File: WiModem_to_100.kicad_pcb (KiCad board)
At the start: 2 copper layers, 12.3 x 34.7 mm, 2 parts, among them J1 DB25_Male, J2 DB25_Male

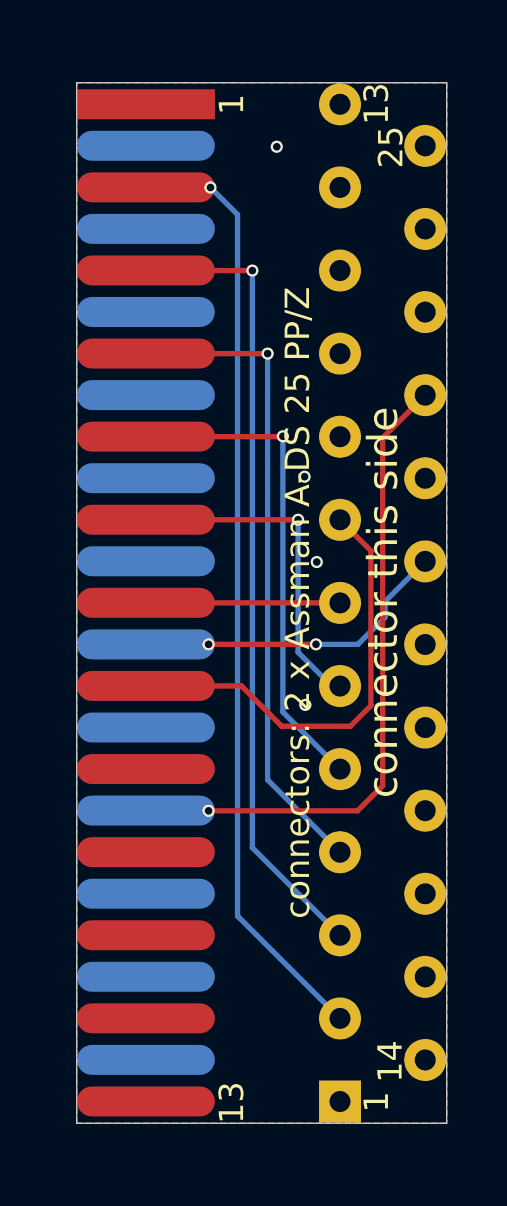
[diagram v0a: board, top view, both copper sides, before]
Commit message: tiny adjustments to routing and ground plane connections
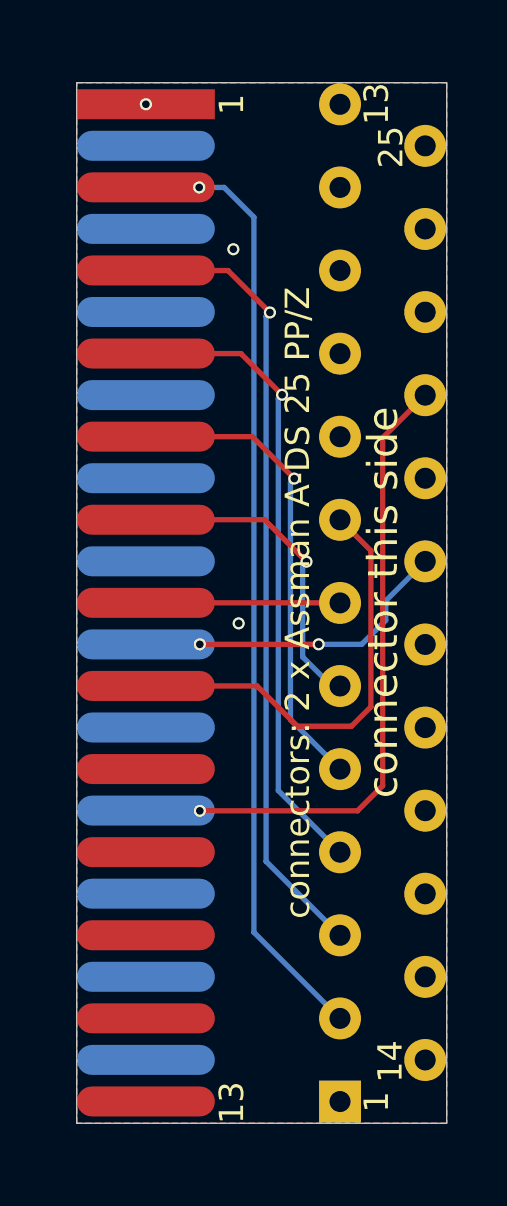
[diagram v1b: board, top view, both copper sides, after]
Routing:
- net /TXD: track 29.5 -> 31.9 mm
- net /DSR: track 10.6 -> 10.0 mm
- net /CTS: track 15.7 -> 15.2 mm
- net GND: vias 4 -> 3

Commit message: widen through-holes, improve readme
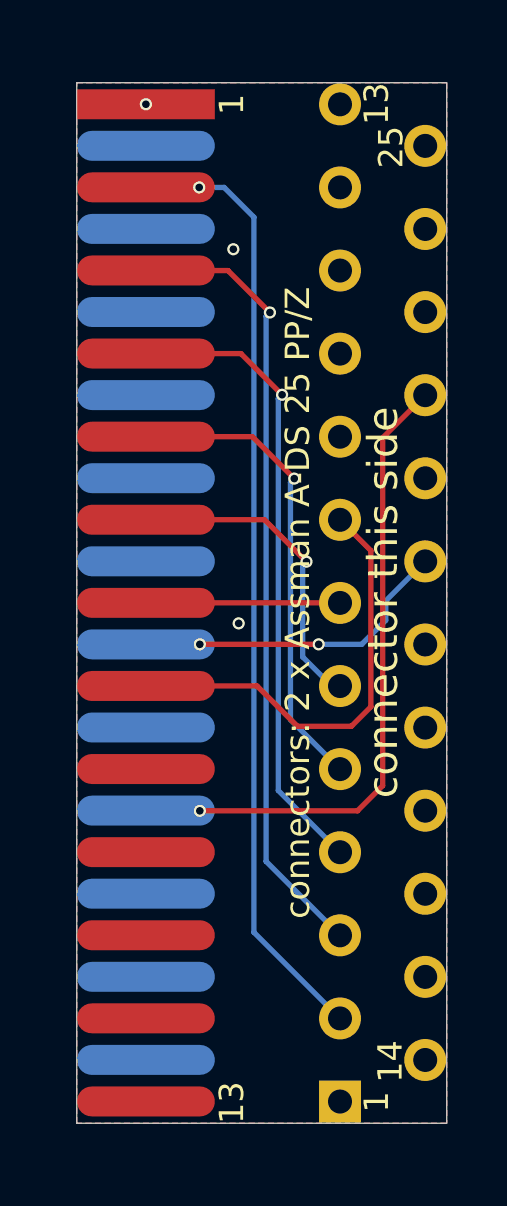
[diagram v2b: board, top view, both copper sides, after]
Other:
- rule pad_to_mask_clearance: 0.051 -> 0
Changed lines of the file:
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@@
     (35 F.Paste user hide)
     (36 B.SilkS user)
-    (37 F.SilkS user hide)
+    (37 F.SilkS user)
     (38 B.Mask user)
-    (39 F.Mask user hide)
+    (39 F.Mask user)
     (40 Dwgs.User user hide)
     (41 Cmts.User user hide)
@@
     (mod_text_size 1 1)
     (mod_text_width 0.15)
-    (pad_size 1.524 1.524)
-    (pad_drill 0.762)
-    (pad_to_mask_clearance 0.051)
-    (solder_mask_min_width 0.25)
+    (pad_size 1.4 1.4)
+    (pad_drill 0.8)
+    (pad_to_mask_clearance 0)
     (aux_axis_origin 0 0)
     (visible_elements FFFFFF7F)
@@
     (fp_arc (start 42.17 -3.83) (end 42.17 -4.83) (angle 90) (layer F.Fab) (width 0.1))
     (fp_arc (start -8.93 -3.83) (end -9.93 -3.83) (angle 90) (layer F.Fab) (width 0.1))
-    (pad 25 thru_hole circle (at 31.855 2.84 90) (size 1.4 1.4) (drill 0.7) (layers *.Cu *.Mask))
-    (pad 24 thru_hole circle (at 29.085 2.84 90) (size 1.4 1.4) (drill 0.7) (layers *.Cu *.Mask))
-    (pad 23 thru_hole circle (at 26.315 2.84 90) (size 1.4 1.4) (drill 0.7) (layers *.Cu *.Mask))
-    (pad 22 thru_hole circle (at 23.545 2.84 90) (size 1.4 1.4) (drill 0.7) (layers *.Cu *.Mask)
+    (pad 25 thru_hole circle (at 31.855 2.84 90) (size 1.4 1.4) (drill 0.8) (layers *.Cu *.Mask))
+    (pad 24 thru_hole circle (at 29.085 2.84 90) (size 1.4 1.4) (drill 0.8) (layers *.Cu *.Mask))
+    (pad 23 thru_hole circle (at 26.315 2.84 90) (size 1.4 1.4) (drill 0.8) (layers *.Cu *.Mask))
+    (pad 22 thru_hole circle (at 23.545 2.84 90) (size 1.4 1.4) (drill 0.8) (layers *.Cu *.Mask)
       (net 1 /RI))
-    (pad 21 thru_hole circle (at 20.775 2.84 90) (size 1.4 1.4) (drill 0.7) (layers *.Cu *.Mask))
-    (pad 20 thru_hole circle (at 18.005 2.84 90) (size 1.4 1.4) (drill 0.7) (layers *.Cu *.Mask)
+    (pad 21 thru_hole circle (at 20.775 2.84 90) (size 1.4 1.4) (drill 0.8) (layers *.Cu *.Mask))
+    (pad 20 thru_hole circle (at 18.005 2.84 90) (size 1.4 1.4) (drill 0.8) (layers *.Cu *.Mask)
       (net 2 /DTR))
-    (pad 19 thru_hole circle (at 15.235 2.84 90) (size 1.4 1.4) (drill 0.7) (layers *.Cu *.Mask))
-    (pad 18 thru_hole circle (at 12.465 2.84 90) (size 1.4 1.4) (drill 0.7) (layers *.Cu *.Mask))
-    (pad 17 thru_hole circle (at 9.695 2.84 90) (size 1.4 1.4) (drill 0.7) (layers *.Cu *.Mask))
-    (pad 16 thru_hole circle (at 6.925 2.84 90) (size 1.4 1.4) (drill 0.7) (layers *.Cu *.Mask))
-    (pad 15 thru_hole circle (at 4.155 2.84 90) (size 1.4 1.4) (drill 0.7) (layers *.Cu *.Mask))
-    (pad 14 thru_hole circle (at 1.385 2.84 90) (size 1.4 1.4) (drill 0.7) (layers *.Cu *.Mask))
-    (pad 13 thru_hole circle (at 33.24 0 90) (size 1.4 1.4) (drill 0.7) (layers *.Cu *.Mask))
-    (pad 12 thru_hole circle (at 30.47 0 90) (size 1.4 1.4) (drill 0.7) (layers *.Cu *.Mask))
-    (pad 11 thru_hole circle (at 27.7 0 90) (size 1.4 1.4) (drill 0.7) (layers *.Cu *.Mask))
-    (pad 10 thru_hole circle (at 24.93 0 90) (size 1.4 1.4) (drill 0.7) (layers *.Cu *.Mask))
-    (pad 9 thru_hole circle (at 22.16 0 90) (size 1.4 1.4) (drill 0.7) (layers *.Cu *.Mask))
-    (pad 8 thru_hole circle (at 19.39 0 90) (size 1.4 1.4) (drill 0.7) (layers *.Cu *.Mask)
+    (pad 19 thru_hole circle (at 15.235 2.84 90) (size 1.4 1.4) (drill 0.8) (layers *.Cu *.Mask))
+    (pad 18 thru_hole circle (at 12.465 2.84 90) (size 1.4 1.4) (drill 0.8) (layers *.Cu *.Mask))
+    (pad 17 thru_hole circle (at 9.695 2.84 90) (size 1.4 1.4) (drill 0.8) (layers *.Cu *.Mask))
+    (pad 16 thru_hole circle (at 6.925 2.84 90) (size 1.4 1.4) (drill 0.8) (layers *.Cu *.Mask))
+    (pad 15 thru_hole circle (at 4.155 2.84 90) (size 1.4 1.4) (drill 0.8) (layers *.Cu *.Mask))
+    (pad 14 thru_hole circle (at 1.385 2.84 90) (size 1.4 1.4) (drill 0.8) (layers *.Cu *.Mask))
+    (pad 13 thru_hole circle (at 33.24 0 90) (size 1.4 1.4) (drill 0.8) (layers *.Cu *.Mask))
+    (pad 12 thru_hole circle (at 30.47 0 90) (size 1.4 1.4) (drill 0.8) (layers *.Cu *.Mask))
+    (pad 11 thru_hole circle (at 27.7 0 90) (size 1.4 1.4) (drill 0.8) (layers *.Cu *.Mask))
+    (pad 10 thru_hole circle (at 24.93 0 90) (size 1.4 1.4) (drill 0.8) (layers *.Cu *.Mask))
+    (pad 9 thru_hole circle (at 22.16 0 90) (size 1.4 1.4) (drill 0.8) (layers *.Cu *.Mask))
+    (pad 8 thru_hole circle (at 19.39 0 90) (size 1.4 1.4) (drill 0.8) (layers *.Cu *.Mask)
       (net 3 /DCD))
-    (pad 7 thru_hole circle (at 16.62 0 90) (size 1.4 1.4) (drill 0.7) (layers *.Cu *.Mask)
+    (pad 7 thru_hole circle (at 16.62 0 90) (size 1.4 1.4) (drill 0.8) (layers *.Cu *.Mask)
       (net 4 /SG))
-    (pad 6 thru_hole circle (at 13.85 0 90) (size 1.4 1.4) (drill 0.7) (layers *.Cu *.Mask)
+    (pad 6 thru_hole circle (at 13.85 0 90) (size 1.4 1.4) (drill 0.8) (layers *.Cu *.Mask)
       (net 5 /DSR))
-    (pad 5 thru_hole circle (at 11.08 0 90) (size 1.4 1.4) (drill 0.7) (layers *.Cu *.Mask)
+    (pad 5 thru_hole circle (at 11.08 0 90) (size 1.4 1.4) (drill 0.8) (layers *.Cu *.Mask)
       (net 6 /CTS))
-    (pad 4 thru_hole circle (at 8.31 0 90) (size 1.4 1.4) (drill 0.7) (layers *.Cu *.Mask)
+    (pad 4 thru_hole circle (at 8.31 0 90) (size 1.4 1.4) (drill 0.8) (layers *.Cu *.Mask)
       (net 7 /RTS))
-    (pad 3 thru_hole circle (at 5.54 0 90) (size 1.4 1.4) (drill 0.7) (layers *.Cu *.Mask)
+    (pad 3 thru_hole circle (at 5.54 0 90) (size 1.4 1.4) (drill 0.8) (layers *.Cu *.Mask)
       (net 8 /RXD))
-    (pad 2 thru_hole circle (at 2.77 0 90) (size 1.4 1.4) (drill 0.7) (layers *.Cu *.Mask)
+    (pad 2 thru_hole circle (at 2.77 0 90) (size 1.4 1.4) (drill 0.8) (layers *.Cu *.Mask)
       (net 9 /TXD))
-    (pad 1 thru_hole rect (at 0 0 90) (size 1.4 1.4) (drill 0.7) (layers *.Cu *.Mask)
+    (pad 1 thru_hole rect (at 0 0 90) (size 1.4 1.4) (drill 0.8) (layers *.Cu *.Mask)
       (net 10 GND))
     (model ${KIPRJMOD}/0_LOCAL.3dshapes/connector_a-ds_25_pp_z.stp
@@
   (gr_line (start 135.4455 79.0829) (end 147.7772 79.0829) (layer Edge.Cuts) (width 0.0254))
   (gr_line (start 147.7772 113.7666) (end 147.7772 79.0829) (layer Edge.Cuts) (width 0.0254))
-  (via (at 140.6652 84.6328) (size 0.4064) (drill 0.254) (layers F.Cu B.Cu) (net 10))
   (segment (start 139.5476 103.3526) (end 144.8054 103.3526) (width 0.1778) (layer F.Cu) (net 1))
   (via (at 139.5476 103.3526) (size 0.4064) (drill 0.254) (layers F.Cu B.Cu) (net 1))
@@
   (segment (start 141.351 83.566) (end 141.351 107.4025) (width 0.1778) (layer B.Cu) (net 9))
   (segment (start 140.35786 82.57286) (end 141.351 83.566) (width 0.1778) (layer B.Cu) (net 9))
+  (via (at 140.6652 84.6328) (size 0.4064) (drill 0.254) (layers F.Cu B.Cu) (net 10))
   (via (at 140.843 97.1042) (size 0.4064) (drill 0.254) (layers F.Cu B.Cu) (net 10))
   (via (at 137.75 79.8) (size 0.4064) (drill 0.254) (layers F.Cu B.Cu) (net 10))

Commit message: edge connector too close to normal connector
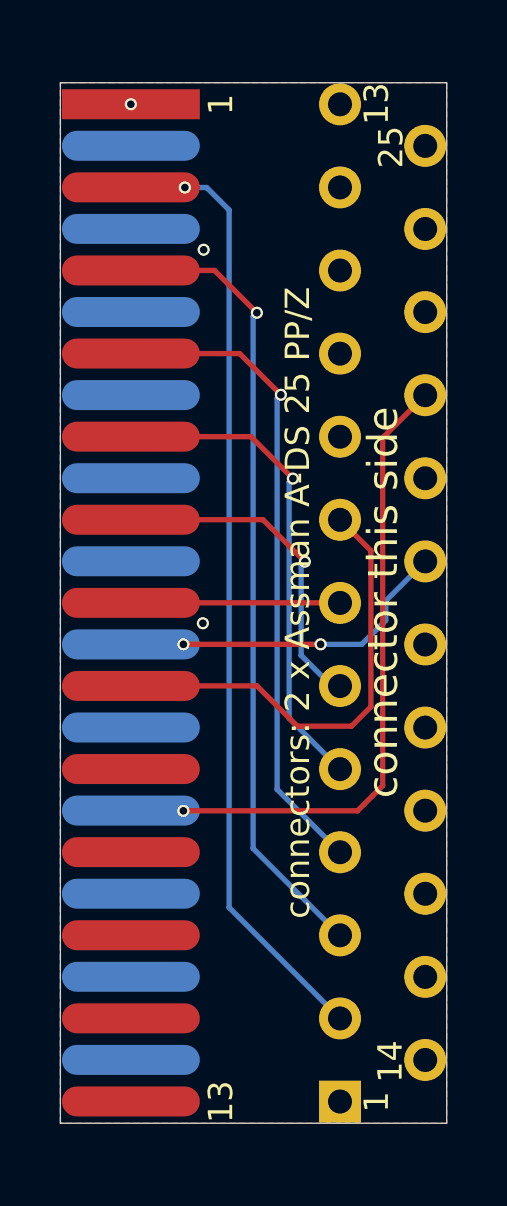
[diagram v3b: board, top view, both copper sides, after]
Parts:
- moved J1 0.50 mm to (136.8, 96.4)
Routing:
- net /RTS: track 20.5 -> 23.0 mm
- net /RXD: track 24.4 -> 26.8 mm
- net /TXD: track 31.9 -> 30.3 mm
- net /CTS: track 15.2 -> 16.4 mm
- net /DSR: track 10.0 -> 11.3 mm
- net /RI: track 20.0 -> 20.6 mm
- net /DTR: track 9.04 -> 9.59 mm
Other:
- board size 12.3 x 34.7 mm -> 12.9 x 34.7 mm

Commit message: larger drills
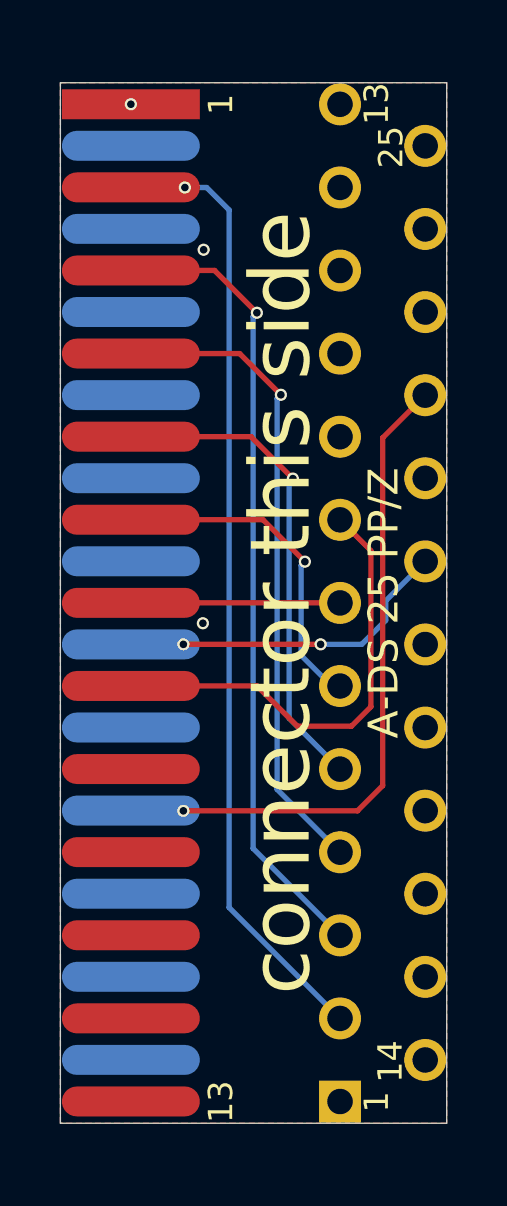
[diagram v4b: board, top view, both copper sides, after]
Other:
- board text added: "A-DS 25 PP/Z"
- board text added: "github.com/bkw777/WiModem_to_100"
- board text removed: "connectors: 2 x Assman A-DS 25 PP/Z"
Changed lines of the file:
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@@
   (general
     (thickness 1.6)
-    (drawings 20)
+    (drawings 21)
     (tracks 56)
     (zones 0)
@@
   )
   (setup
-    (last_trace_width 0.1778)
+    (last_trace_width 0.25)
     (user_trace_width 0.1778)
     (trace_clearance 0.2)
@@
     (fp_arc (start 42.17 -3.83) (end 42.17 -4.83) (angle 90) (layer F.Fab) (width 0.1))
     (fp_arc (start -8.93 -3.83) (end -9.93 -3.83) (angle 90) (layer F.Fab) (width 0.1))
-    (pad 25 thru_hole circle (at 31.855 2.84 90) (size 1.4 1.4) (drill 0.8) (layers *.Cu *.Mask))
-    (pad 24 thru_hole circle (at 29.085 2.84 90) (size 1.4 1.4) (drill 0.8) (layers *.Cu *.Mask))
-    (pad 23 thru_hole circle (at 26.315 2.84 90) (size 1.4 1.4) (drill 0.8) (layers *.Cu *.Mask))
-    (pad 22 thru_hole circle (at 23.545 2.84 90) (size 1.4 1.4) (drill 0.8) (layers *.Cu *.Mask)
+    (pad 25 thru_hole circle (at 31.855 2.84 90) (size 1.4 1.4) (drill 0.85) (layers *.Cu *.Mask))
+    (pad 24 thru_hole circle (at 29.085 2.84 90) (size 1.4 1.4) (drill 0.85) (layers *.Cu *.Mask))
+    (pad 23 thru_hole circle (at 26.315 2.84 90) (size 1.4 1.4) (drill 0.85) (layers *.Cu *.Mask))
+    (pad 22 thru_hole circle (at 23.545 2.84 90) (size 1.4 1.4) (drill 0.85) (layers *.Cu *.Mask)
       (net 1 /RI))
-    (pad 21 thru_hole circle (at 20.775 2.84 90) (size 1.4 1.4) (drill 0.8) (layers *.Cu *.Mask))
-    (pad 20 thru_hole circle (at 18.005 2.84 90) (size 1.4 1.4) (drill 0.8) (layers *.Cu *.Mask)
+    (pad 21 thru_hole circle (at 20.775 2.84 90) (size 1.4 1.4) (drill 0.85) (layers *.Cu *.Mask))
+    (pad 20 thru_hole circle (at 18.005 2.84 90) (size 1.4 1.4) (drill 0.85) (layers *.Cu *.Mask)
       (net 2 /DTR))
-    (pad 19 thru_hole circle (at 15.235 2.84 90) (size 1.4 1.4) (drill 0.8) (layers *.Cu *.Mask))
-    (pad 18 thru_hole circle (at 12.465 2.84 90) (size 1.4 1.4) (drill 0.8) (layers *.Cu *.Mask))
-    (pad 17 thru_hole circle (at 9.695 2.84 90) (size 1.4 1.4) (drill 0.8) (layers *.Cu *.Mask))
-    (pad 16 thru_hole circle (at 6.925 2.84 90) (size 1.4 1.4) (drill 0.8) (layers *.Cu *.Mask))
-    (pad 15 thru_hole circle (at 4.155 2.84 90) (size 1.4 1.4) (drill 0.8) (layers *.Cu *.Mask))
-    (pad 14 thru_hole circle (at 1.385 2.84 90) (size 1.4 1.4) (drill 0.8) (layers *.Cu *.Mask))
-    (pad 13 thru_hole circle (at 33.24 0 90) (size 1.4 1.4) (drill 0.8) (layers *.Cu *.Mask))
-    (pad 12 thru_hole circle (at 30.47 0 90) (size 1.4 1.4) (drill 0.8) (layers *.Cu *.Mask))
-    (pad 11 thru_hole circle (at 27.7 0 90) (size 1.4 1.4) (drill 0.8) (layers *.Cu *.Mask))
-    (pad 10 thru_hole circle (at 24.93 0 90) (size 1.4 1.4) (drill 0.8) (layers *.Cu *.Mask))
-    (pad 9 thru_hole circle (at 22.16 0 90) (size 1.4 1.4) (drill 0.8) (layers *.Cu *.Mask))
-    (pad 8 thru_hole circle (at 19.39 0 90) (size 1.4 1.4) (drill 0.8) (layers *.Cu *.Mask)
+    (pad 19 thru_hole circle (at 15.235 2.84 90) (size 1.4 1.4) (drill 0.85) (layers *.Cu *.Mask))
+    (pad 18 thru_hole circle (at 12.465 2.84 90) (size 1.4 1.4) (drill 0.85) (layers *.Cu *.Mask))
+    (pad 17 thru_hole circle (at 9.695 2.84 90) (size 1.4 1.4) (drill 0.85) (layers *.Cu *.Mask))
+    (pad 16 thru_hole circle (at 6.925 2.84 90) (size 1.4 1.4) (drill 0.85) (layers *.Cu *.Mask))
+    (pad 15 thru_hole circle (at 4.155 2.84 90) (size 1.4 1.4) (drill 0.85) (layers *.Cu *.Mask))
+    (pad 14 thru_hole circle (at 1.385 2.84 90) (size 1.4 1.4) (drill 0.85) (layers *.Cu *.Mask))
+    (pad 13 thru_hole circle (at 33.24 0 90) (size 1.4 1.4) (drill 0.85) (layers *.Cu *.Mask))
+    (pad 12 thru_hole circle (at 30.47 0 90) (size 1.4 1.4) (drill 0.85) (layers *.Cu *.Mask))
+    (pad 11 thru_hole circle (at 27.7 0 90) (size 1.4 1.4) (drill 0.85) (layers *.Cu *.Mask))
+    (pad 10 thru_hole circle (at 24.93 0 90) (size 1.4 1.4) (drill 0.85) (layers *.Cu *.Mask))
+    (pad 9 thru_hole circle (at 22.16 0 90) (size 1.4 1.4) (drill 0.85) (layers *.Cu *.Mask))
+    (pad 8 thru_hole circle (at 19.39 0 90) (size 1.4 1.4) (drill 0.85) (layers *.Cu *.Mask)
       (net 3 /DCD))
-    (pad 7 thru_hole circle (at 16.62 0 90) (size 1.4 1.4) (drill 0.8) (layers *.Cu *.Mask)
+    (pad 7 thru_hole circle (at 16.62 0 90) (size 1.4 1.4) (drill 0.85) (layers *.Cu *.Mask)
       (net 4 /SG))
-    (pad 6 thru_hole circle (at 13.85 0 90) (size 1.4 1.4) (drill 0.8) (layers *.Cu *.Mask)
+    (pad 6 thru_hole circle (at 13.85 0 90) (size 1.4 1.4) (drill 0.85) (layers *.Cu *.Mask)
       (net 5 /DSR))
-    (pad 5 thru_hole circle (at 11.08 0 90) (size 1.4 1.4) (drill 0.8) (layers *.Cu *.Mask)
+    (pad 5 thru_hole circle (at 11.08 0 90) (size 1.4 1.4) (drill 0.85) (layers *.Cu *.Mask)
       (net 6 /CTS))
-    (pad 4 thru_hole circle (at 8.31 0 90) (size 1.4 1.4) (drill 0.8) (layers *.Cu *.Mask)
+    (pad 4 thru_hole circle (at 8.31 0 90) (size 1.4 1.4) (drill 0.85) (layers *.Cu *.Mask)
       (net 7 /RTS))
-    (pad 3 thru_hole circle (at 5.54 0 90) (size 1.4 1.4) (drill 0.8) (layers *.Cu *.Mask)
+    (pad 3 thru_hole circle (at 5.54 0 90) (size 1.4 1.4) (drill 0.85) (layers *.Cu *.Mask)
       (net 8 /RXD))
-    (pad 2 thru_hole circle (at 2.77 0 90) (size 1.4 1.4) (drill 0.8) (layers *.Cu *.Mask)
+    (pad 2 thru_hole circle (at 2.77 0 90) (size 1.4 1.4) (drill 0.85) (layers *.Cu *.Mask)
       (net 9 /TXD))
-    (pad 1 thru_hole rect (at 0 0 90) (size 1.4 1.4) (drill 0.8) (layers *.Cu *.Mask)
+    (pad 1 thru_hole rect (at 0 0 90) (size 1.4 1.4) (drill 0.85) (layers *.Cu *.Mask)
       (net 10 GND))
     (model ${KIPRJMOD}/0_LOCAL.3dshapes/connector_a-ds_25_pp_z.stp
@@
     )
   )
+  (gr_text github.com/bkw777/WiModem_to_100 (at 145.65 96.4 90) (layer B.SilkS)
+    (effects (font (size 0.8 0.8) (thickness 0.1)) (justify mirror))
+  )
   (gr_text 25 (at 145.923 81.2292 90) (layer B.SilkS)
     (effects (font (size 0.8128 0.8128) (thickness 0.1016)) (justify mirror))
@@
     (effects (font (size 0.8128 0.8128) (thickness 0.1016)))
   )
-  (gr_text "connectors: 2 x Assman A-DS 25 PP/Z" (at 142.8115 96.4184 90) (layer F.SilkS)
-    (effects (font (size 0.8128 0.8128) (thickness 0.1016)))
-  )
-  (gr_text "connector this side" (at 145.6563 96.4057 90) (layer F.SilkS)
-    (effects (font (size 1 1) (thickness 0.15)))
-  )
-  (gr_text "TRS-80 Model 100" (at 145.6944 96.4311 90) (layer B.SilkS)
+  (gr_text "A-DS 25 PP/Z" (at 145.675 96.425 90) (layer F.SilkS)
+    (effects (font (size 1 1) (thickness 0.1)))
+  )
+  (gr_text "connector this side" (at 142.25 96.425 90) (layer F.SilkS)
+    (effects (font (size 2 2) (thickness 0.2)))
+  )
+  (gr_text "TRS-80 Model 100" (at 142.425 96.4311 90) (layer B.SilkS)
     (effects (font (size 1.2192 1.2192) (thickness 0.1524)) (justify mirror))
   )
@@
   (gr_line (start 134.9 79.0829) (end 147.7772 79.0829) (layer Edge.Cuts) (width 0.0254))
   (gr_line (start 147.7772 113.7666) (end 147.7772 79.0829) (layer Edge.Cuts) (width 0.0254))
-  (via (at 139.05 82.575) (size 0.4064) (drill 0.254) (layers F.Cu B.Cu) (net 9))
   (segment (start 147.0612 89.5017) (end 147.0612 89.4977) (width 0.1778) (layer F.Cu) (net 1))
   (segment (start 139 103.3526) (end 144.8054 103.3526) (width 0.1778) (layer F.Cu) (net 1))
@@
   (segment (start 140.04 85.34) (end 137.25 85.34) (width 0.1778) (layer F.Cu) (net 8))
   (segment (start 141.325 86.875) (end 141.325 104.6065) (width 0.1778) (layer B.Cu) (net 8))
+  (via (at 139.05 82.575) (size 0.4064) (drill 0.254) (layers F.Cu B.Cu) (net 9))
   (segment (start 144.2212 110.2727) (end 144.2198 110.2727) (width 0.1778) (layer F.Cu) (net 9))
   (segment (start 140.525 106.5765) (end 144.2212 110.2727) (width 0.1778) (layer B.Cu) (net 9))
